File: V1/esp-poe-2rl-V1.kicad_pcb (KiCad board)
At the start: 4 copper layers, 88 x 45 mm, 91 parts, among them J1 USB_C_Receptacle_USB2.0, J2 1x2P 5,08mm, J3 1x2P 5,08mm, J4 RJ45 JACK, K1 G5NB-1A-E-DC5, K2 G5NB-1A-E-DC5, Q1 WPM2015-3/TR, Q2 LMUN2211LT1G, Q3 UMH3N, Q4 MMBT2222A, Q5 MMBT2222A, SW1 RESET, U1 CH340K, U2 ESP32-WROOM-32UE-N16, U3 LAN8710A, U4 TX4138, U5 SY8089A1AAC, U6 TPS2376DDAR-H

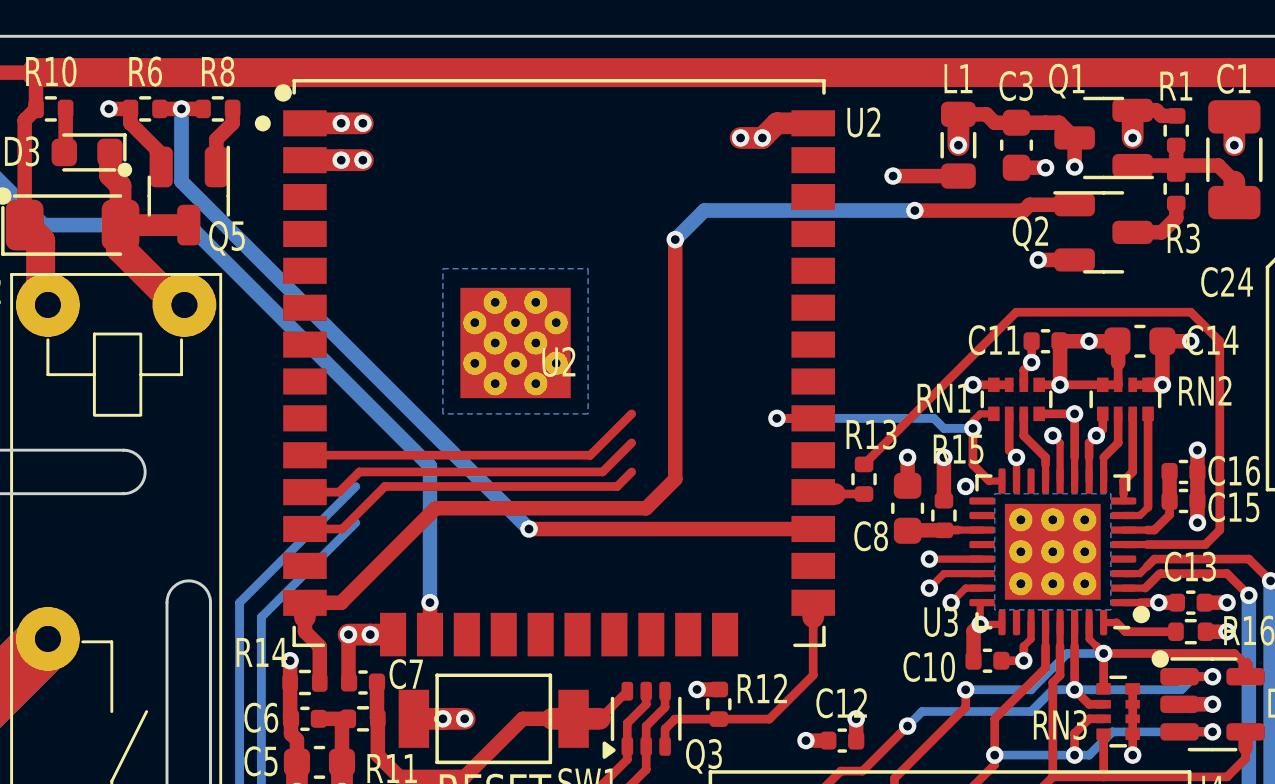
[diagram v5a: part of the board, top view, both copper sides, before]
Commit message: Rerouting
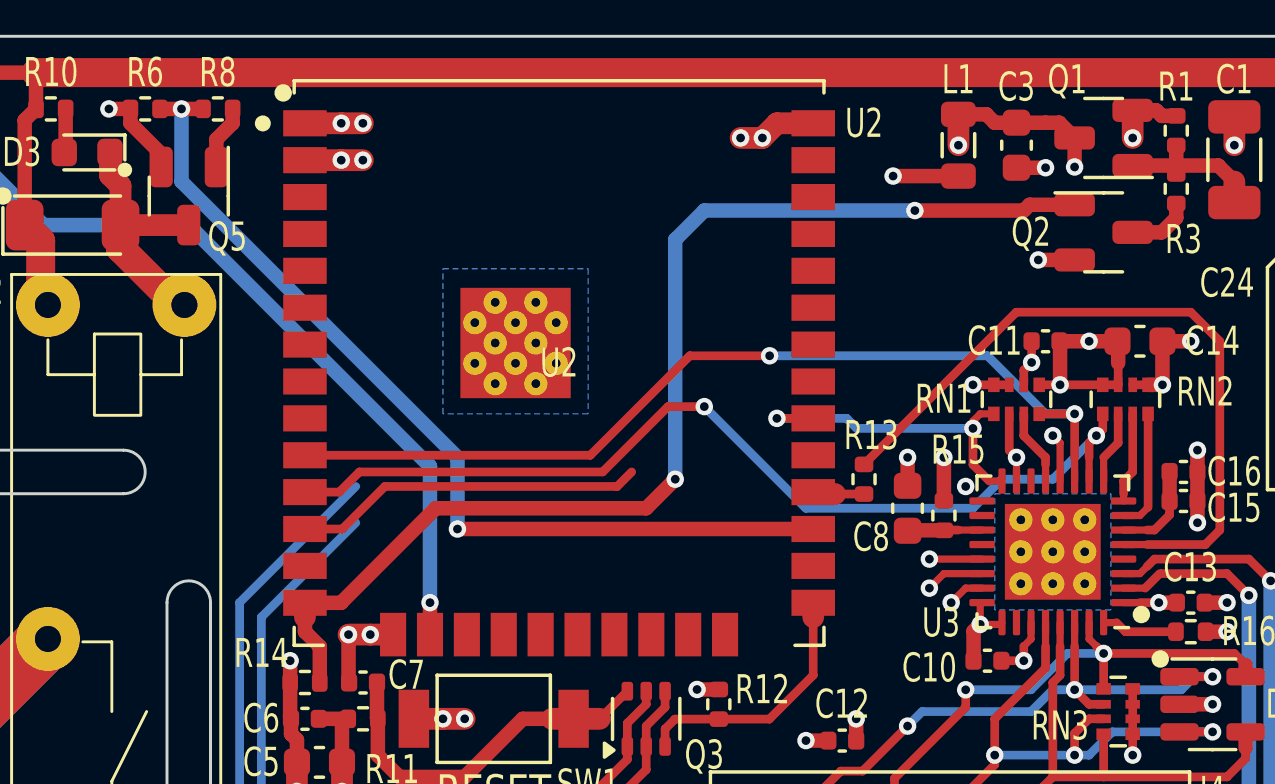
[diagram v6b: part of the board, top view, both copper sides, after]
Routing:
- net /EMACRXD1: track 14.5 -> 33.5 mm, vias 1 -> 2
- net /EMACRXD0: track 15.4 -> 32.3 mm, vias 1 -> 2
- net OUT2: track 30.7 -> 32.1 mm
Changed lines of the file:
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@@
 	(segment
 		(start 123 87.965)
-		(end 113.215 87.965)
+		(end 110.75 87.965)
 		(width 0.5)
 		(layer "F.Cu")
@@
 	)
 	(via
-		(at 113.215 87.965)
+		(at 110.75 87.965)
 		(size 0.6)
 		(drill 0.3)
@@
 	)
 	(segment
-		(start 113.215 87.965)
-		(end 101.25 76)
+		(start 110.75 87.965)
+		(end 110.75 85.5)
 		(width 0.5)
 		(layer "B.Cu")
@@
 		(start 101.25 76)
 		(end 101.25 73.5)
+		(width 0.5)
+		(layer "B.Cu")
+		(net 51)
+	)
+	(segment
+		(start 110.75 85.5)
+		(end 101.25 76)
 		(width 0.5)
 		(layer "B.Cu")
@@
 	)
 	(segment
-		(start 110 87.25)
-		(end 117.25 87.25)
-		(width 0.5)
-		(layer "F.Cu")
-		(net 53)
-	)
-	(segment
 		(start 105.5 91)
 		(end 105.5 91.5)
@@
 	)
 	(segment
+		(start 110 87.25)
+		(end 106.745 90.505)
+		(width 0.5)
+		(layer "F.Cu")
+		(net 53)
+	)
+	(segment
+		(start 118.25 86.25)
+		(end 117.25 87.25)
+		(width 0.5)
+		(layer "F.Cu")
+		(net 53)
+	)
+	(segment
 		(start 117.25 87.25)
-		(end 118.25 86.25)
-		(width 0.5)
-		(layer "F.Cu")
-		(net 53)
-	)
-	(segment
-		(start 105.5 90.505)
-		(end 106.745 90.505)
-		(width 0.5)
-		(layer "F.Cu")
-		(net 53)
-	)
-	(segment
-		(start 106.745 90.505)
 		(end 110 87.25)
 		(width 0.5)
@@
 		(start 130.25 77)
 		(end 130.45 76.8)
-		(width 0.5)
-		(layer "F.Cu")
-		(net 53)
-	)
-	(segment
-		(start 118.25 86.25)
-		(end 118.25 78)
 		(width 0.5)
 		(layer "F.Cu")
@@
 	)
 	(segment
+		(start 106.745 90.505)
+		(end 105.5 90.505)
+		(width 0.5)
+		(layer "F.Cu")
+		(net 53)
+	)
+	(segment
 		(start 105.5 91.5)
 		(end 106.01 92.01)
@@
 	)
 	(via
-		(at 118.25 78)
-		(size 0.6)
-		(drill 0.3)
-		(layers "F.Cu" "B.Cu")
-		(net 53)
-	)
-	(segment
-		(start 126.5 77)
+		(at 118.25 86.25)
+		(size 0.6)
+		(drill 0.3)
+		(layers "F.Cu" "B.Cu")
+		(net 53)
+	)
+	(segment
+		(start 119.25 77)
+		(end 126.5 77)
+		(width 0.5)
+		(layer "B.Cu")
+		(net 53)
+	)
+	(segment
+		(start 118.25 86.25)
+		(end 118.25 78)
+		(width 0.5)
+		(layer "B.Cu")
+		(net 53)
+	)
+	(segment
+		(start 118.25 78)
 		(end 119.25 77)
-		(width 0.5)
-		(layer "B.Cu")
-		(net 53)
-	)
-	(segment
-		(start 119.25 77)
-		(end 118.25 78)
 		(width 0.5)
 		(layer "B.Cu")
@@
 	)
 	(segment
+		(start 115.325 85.425)
+		(end 105.5 85.425)
+		(width 0.3)
+		(layer "F.Cu")
+		(net 77)
+	)
+	(segment
+		(start 121.5 82)
+		(end 118.75 82)
+		(width 0.3)
+		(layer "F.Cu")
+		(net 77)
+	)
+	(segment
 		(start 132 85.5)
 		(end 132 86.3125)
@@
 	)
 	(segment
-		(start 105.5 85.425)
+		(start 118.75 82)
 		(end 115.325 85.425)
 		(width 0.3)
@@
 		(net 77)
 	)
-	(segment
-		(start 115.325 85.425)
-		(end 116.75 84)
-		(width 0.3)
-		(layer "F.Cu")
+	(via
+		(at 121.5 82)
+		(size 0.6)
+		(drill 0.3)
+		(layers "F.Cu" "B.Cu")
 		(net 77)
 	)
@@
 		(drill 0.3)
 		(layers "F.Cu" "B.Cu")
+		(net 77)
+	)
+	(segment
+		(start 131 84)
+		(end 132 84)
+		(width 0.3)
+		(layer "B.Cu")
+		(net 77)
+	)
+	(segment
+		(start 129 82)
+		(end 131 84)
+		(width 0.3)
+		(layer "B.Cu")
+		(net 77)
+	)
+	(segment
+		(start 121.5 82)
+		(end 129 82)
+		(width 0.3)
+		(layer "B.Cu")
 		(net 77)
 	)
@@
 	)
 	(segment
-		(start 127.5 84.5)
+		(start 124.5 84.5)
 		(end 128.5 84.5)
 		(width 0.3)
@@
 	(segment
 		(start 121.75 84.155)
-		(end 127.155 84.155)
-		(width 0.3)
-		(layer "B.Cu")
-		(net 79)
-	)
-	(segment
-		(start 127.155 84.155)
-		(end 127.5 84.5)
+		(end 124.155 84.155)
+		(width 0.3)
+		(layer "B.Cu")
+		(net 79)
+	)
+	(segment
+		(start 124.155 84.155)
+		(end 124.5 84.5)
 		(width 0.3)
 		(layer "B.Cu")
@@
 	)
 	(segment
+		(start 106.68 86.695)
+		(end 105.5 86.695)
+		(width 0.3)
+		(layer "F.Cu")
+		(net 93)
+	)
+	(segment
+		(start 107.375 86)
+		(end 106.68 86.695)
+		(width 0.3)
+		(layer "F.Cu")
+		(net 93)
+	)
+	(segment
 		(start 132.75 84.75)
 		(end 132.97 84.53)
@@
 	)
 	(segment
-		(start 107.375 86)
-		(end 115.75 86)
-		(width 0.3)
-		(layer "F.Cu")
-		(net 93)
-	)
-	(segment
-		(start 105.5 86.695)
-		(end 106.68 86.695)
-		(width 0.3)
-		(layer "F.Cu")
-		(net 93)
-	)
-	(segment
-		(start 115.75 86)
-		(end 116.75 85)
-		(width 0.3)
-		(layer "F.Cu")
-		(net 93)
-	)
-	(segment
 		(start 132.5 85.5)
 		(end 132.5 85)
@@
 	)
 	(segment
-		(start 106.68 86.695)
+		(start 115.75 86)
 		(end 107.375 86)
+		(width 0.3)
+		(layer "F.Cu")
+		(net 93)
+	)
+	(segment
+		(start 119.25 83.75)
+		(end 118 83.75)
 		(width 0.3)
 		(layer "F.Cu")
@@
 	)
 	(segment
+		(start 118 83.75)
+		(end 115.75 86)
+		(width 0.3)
+		(layer "F.Cu")
+		(net 93)
+	)
+	(segment
 		(start 132.97 84.53)
 		(end 132.97 84)
@@
 	)
 	(via
+		(at 119.25 83.75)
+		(size 0.6)
+		(drill 0.3)
+		(layers "F.Cu" "B.Cu")
+		(net 93)
+	)
+	(via
 		(at 132.75 84.75)
 		(size 0.6)
@@
 		(net 93)
 	)
+	(segment
+		(start 128.5 87.25)
+		(end 129.5 86.25)
+		(width 0.3)
+		(layer "B.Cu")
+		(net 93)
+	)
+	(segment
+		(start 119.25 83.75)
+		(end 122.75 87.25)
+		(width 0.3)
+		(layer "B.Cu")
+		(net 93)
+	)
+	(segment
+		(start 122.75 87.25)
+		(end 128.5 87.25)
+		(width 0.3)
+		(layer "B.Cu")
+		(net 93)
+	)
+	(segment
+		(start 129.5 86.25)
+		(end 131.25 86.25)
+		(width 0.3)
+		(layer "B.Cu")
+		(net 93)
+	)
+	(segment
+		(start 131.25 86.25)
+		(end 132.75 84.75)
+		(width 0.3)
+		(layer "B.Cu")
+		(net 93)
+	)

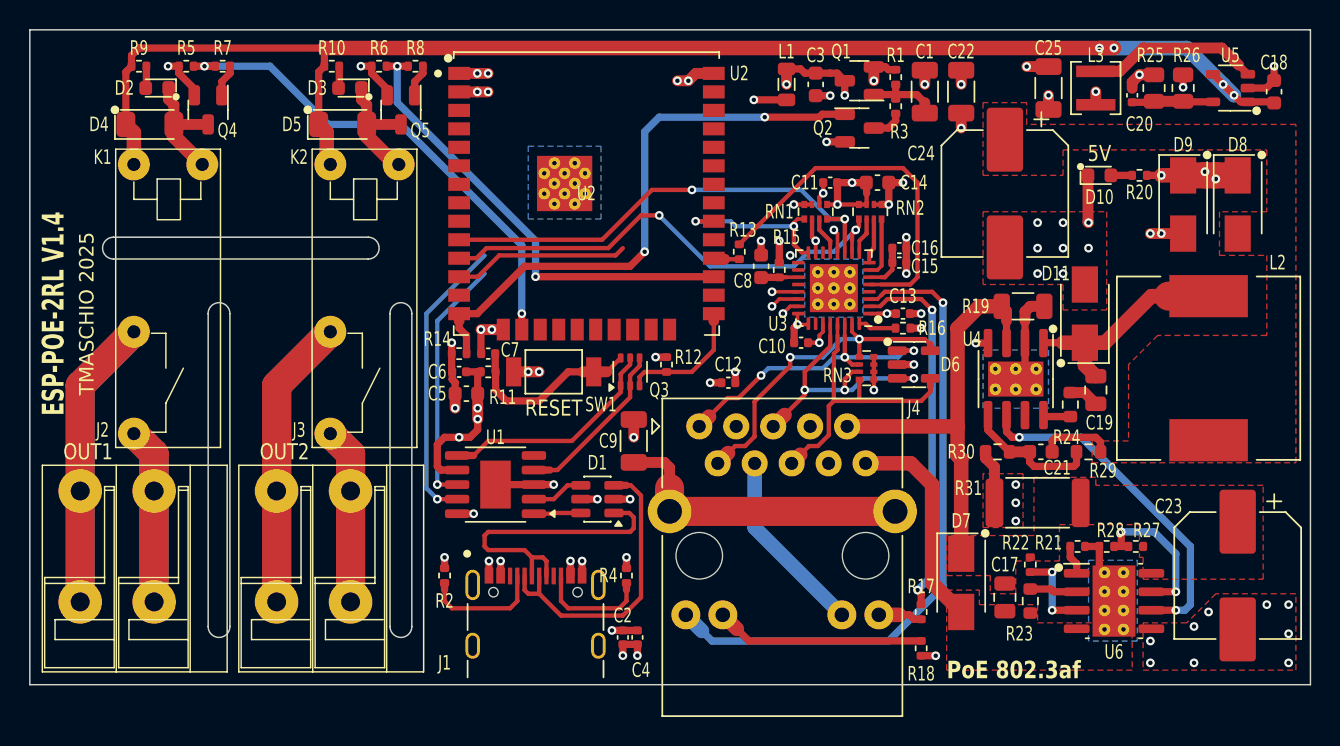
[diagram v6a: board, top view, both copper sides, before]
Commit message: Rerouting
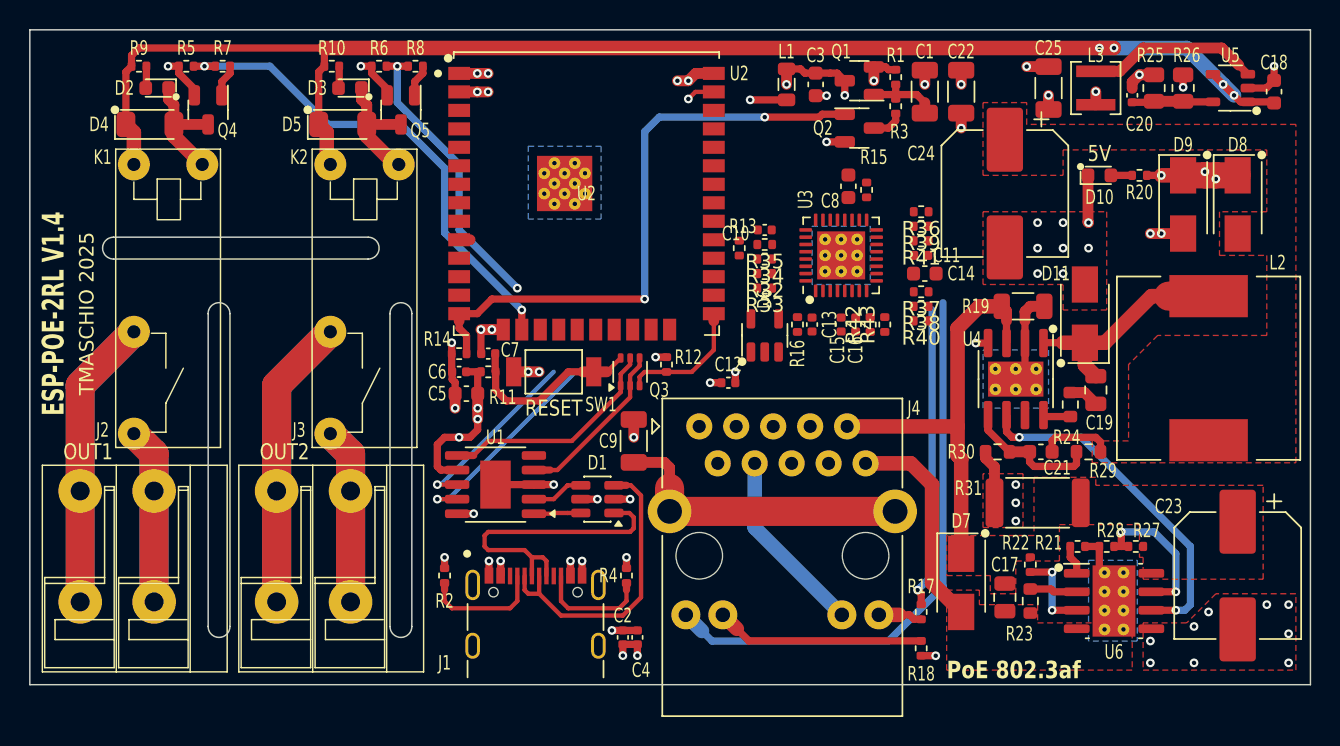
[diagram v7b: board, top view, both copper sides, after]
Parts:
- removed RN1, RN2: 4x2,2k, Tales:R_Array_Convex_4x0402
- removed RN3: 4x49,9R, Tales:R_Array_Convex_4x0402
- added R32: 49,9R, Tales:R_0402_1005Metric, F.Cu at (126.5, 87.8)
- added R33: 49,9R, Tales:R_0402_1005Metric, F.Cu at (126.5, 88.8)
- added R34: 49,9R, Tales:R_0402_1005Metric, F.Cu at (126.5, 86.8)
- added R35: 49,9R, Tales:R_0402_1005Metric, F.Cu at (126.5, 85.8)
- added R36: 2k2, Tales:R_0402_1005Metric, F.Cu at (137.2, 83.5)
- added R37: 2k2, Tales:R_0402_1005Metric, F.Cu at (137.2, 89.0)
- added R38: 2k2, Tales:R_0402_1005Metric, F.Cu at (137.2, 90.0)
- added R39: 2k2, Tales:R_0402_1005Metric, F.Cu at (137.2, 84.5)
- added R40: 2k2, Tales:R_0402_1005Metric, F.Cu at (137.2, 91.0)
- added R41: 2k2, Tales:R_0402_1005Metric, F.Cu at (137.2, 85.5)
- added R42: 2k2, Tales:R_0402_1005Metric, F.Cu at (133.8, 91.2)
- added R43: 2k2, Tales:R_0402_1005Metric, F.Cu at (134.8, 91.2)
- moved D6 10.4 mm to (126.5, 92.0), turned to 90 degrees
- moved C10 8.14 mm to (126.5, 84.8)
- moved C8 8.14 mm to (132.2, 81.8)
- moved R15 8.14 mm to (133.5, 82.0)
- moved C11 8.00 mm to (137.2, 86.5), turned to 0 degrees
- moved R16 7.25 mm to (128.8, 91.2), turned to -90 degrees
- moved C14 7.04 mm to (137.5, 87.8)
- moved C13 6.29 mm to (129.8, 91.2), turned to -90 degrees
- moved C16 6.05 mm to (132.8, 91.2), turned to -90 degrees
- moved C15 5.84 mm to (131.8, 91.2), turned to -90 degrees
- moved U3 2.30 mm to (131.8, 86.5), turned to 90 degrees
- moved R13 0.25 mm to (124.8, 86.0)
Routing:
- net /EMACRXD1: track 33.5 -> 0.00 mm, vias 2 -> 0
- net /EMACRXD0: track 32.3 -> 0.75 mm, vias 2 -> 0
- net /EMACCLK: track 24.9 -> 0.00 mm
- net /ETHRXD+: track 23.0 -> 0.00 mm, vias 2 -> 0
- net /ETHRXD-: track 21.6 -> 0.00 mm, vias 3 -> 0
- net /ETHTXD+: track 20.5 -> 0.00 mm
- net /ETHTXD-: track 19.6 -> 0.00 mm, vias 3 -> 0
- net /EMACRX: track 14.5 -> 0.00 mm, vias 1 -> 0
- net GND: track 65.4 -> 51.0 mm, vias 60 -> 50
- net +3V3LAN: track 18.5 -> 6.40 mm, vias 7 -> 2
- net OUT2: track 32.1 -> 20.1 mm
- net /EMACMDIO: track 11.7 -> 0.00 mm, vias 2 -> 0
- net +3V3A: track 25.3 -> 19.2 mm, vias 5 -> 2
- net /UARTRXD: track 20.1 -> 14.5 mm
- net /ETHLEDY: track 45.0 -> 39.5 mm, vias 1 -> 0
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
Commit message: Rerouting
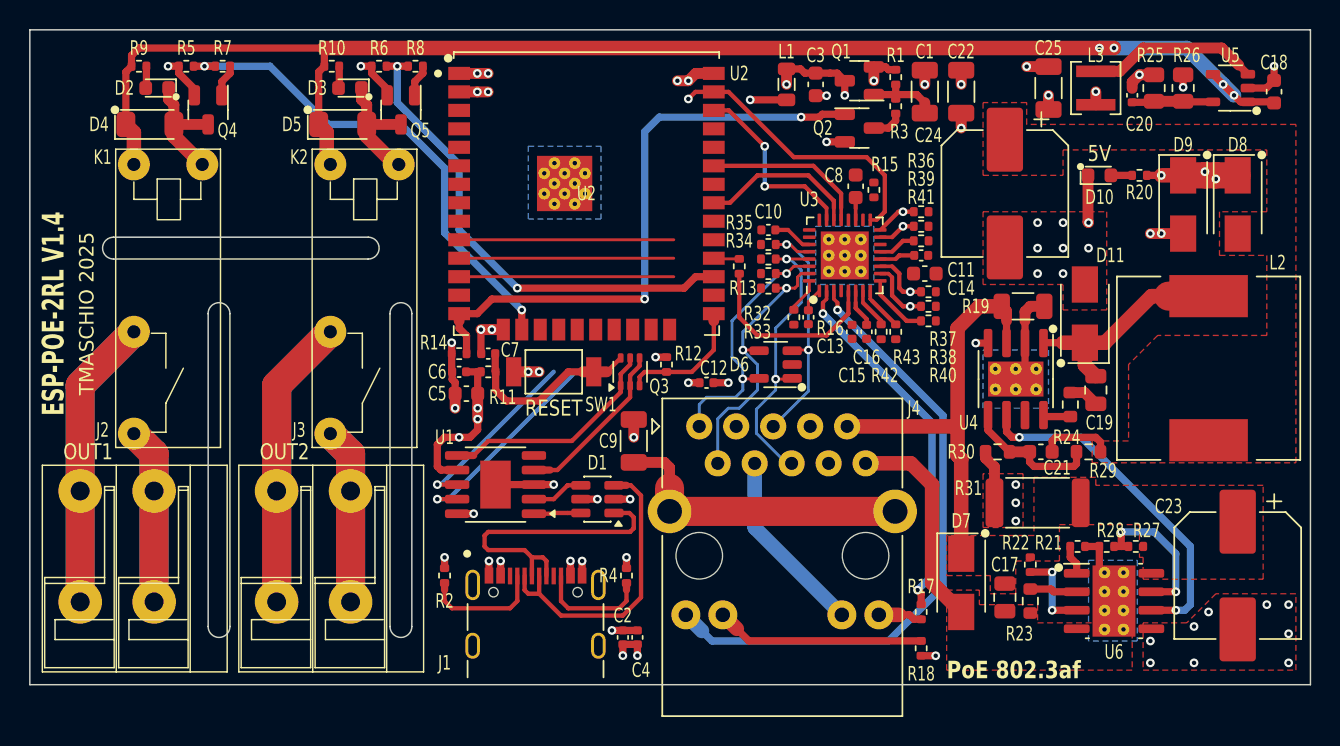
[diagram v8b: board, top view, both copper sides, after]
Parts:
- moved D6 2.14 mm to (127.2, 94.0), turned to 180 degrees
- moved C12 1.50 mm to (122.5, 95.2)
- moved R13 1.25 mm to (124.8, 87.2), turned to -90 degrees
- moved C15 0.90 mm to (132.5, 91.8)
- moved C16 0.90 mm to (133.5, 91.8)
- moved R42 0.90 mm to (134.5, 91.8)
- moved R43 0.90 mm to (135.5, 91.8)
- moved C13 0.56 mm to (129.5, 90.8)
- moved R16 0.56 mm to (128.5, 90.8)
- moved C8 0.50 mm to (132.8, 81.8)
- moved R15 0.50 mm to (134.0, 82.0)
- moved R37 0.50 mm to (137.8, 89.0)
- moved R38 0.50 mm to (137.8, 90.0)
- moved R40 0.50 mm to (137.8, 91.0)
- moved C10 0.25 mm to (126.8, 84.8)
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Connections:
- D6 pad 1: /ETHRXD- -> /ETHTXD+
- D6 pad 4: /ETHTXD+ -> /ETHRXD+
- D6 pad 5: /ETHRXD+ -> /ETHRXD-
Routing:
- net /ETHTXD+: track 0.00 -> 20.5 mm, vias 0 -> 2
- net /ETHRXD+: track 0.00 -> 19.8 mm, vias 0 -> 2
- net /EMACRXD1: track 0.00 -> 19.2 mm, vias 0 -> 1
- net /ETHRXD-: track 0.00 -> 18.7 mm, vias 0 -> 2
- net /EMACRXD0: track 0.75 -> 18.9 mm, vias 0 -> 1
- net /ETHTXD-: track 0.00 -> 17.9 mm, vias 0 -> 2
- net /EMACMDC: track 1.95 -> 19.8 mm
- net /EMACRX: track 0.00 -> 17.4 mm, vias 0 -> 1
- net OUT2: track 20.1 -> 34.0 mm
- net /EMACCLK: track 0.00 -> 13.2 mm
- net /EMACTXD1: track 0.00 -> 13.0 mm, vias 0 -> 2
- net /EMACTXEN: track 0.00 -> 11.4 mm
- net /EMACTXD0: track 0.00 -> 11.1 mm
- net +3V3A: track 19.2 -> 23.9 mm
- net /ETHLEDG: track 20.8 -> 25.3 mm, vias 1 -> 2
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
